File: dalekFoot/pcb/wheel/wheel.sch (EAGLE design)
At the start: 3 parts, among them IC1 LM1117MP-3.3

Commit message: add tb6612fng
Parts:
- added C3: 10uf, rcl:CPOL-US153CLV-0505
- added C4: 100uf, rcl:CPOL-US153CLV-0605
- added IC2: LM1117MP-3.3, lm1117:LM1117MP-3.3
- added U1: TB6612FNG(O,C,8,EL, TB6612FNG:TB6612FNG(O,C,8,EL
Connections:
- removed net VCC-3V3: C2.+, IC1.OUT
- new net VCC-ANALOG: C4.+, IC2.OUT
- new net VCC-DIGITAL: C2.+, IC1.OUT, U1.STBY, U1.VCC
- net BAT+: now also C3.+, IC2.IN
- net DGND: now also C3.-, C4.-, IC2.GND, U1.GND, U1.PGND1@1, U1.PGND1@2, U1.PGND2@1, U1.PGND2@2
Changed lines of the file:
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@@
 <setting verticaltext="up"/>
 </settings>
-<grid distance="0.1" unitdist="inch" unit="mil" style="dots" multiple="1" display="yes" altdistance="0.01" altunitdist="inch" altunit="mil"/>
+<grid distance="0.1" unitdist="inch" unit="inch" style="lines" multiple="1" display="yes" altdistance="0.01" altunitdist="inch" altunit="inch"/>
 <layers>
 <layer number="1" name="Top" color="4" fill="1" visible="no" active="no"/>
@@
 <part name="SUPPLY2" library="supply2" deviceset="DGND" device=""/>
 <part name="SUPPLY3" library="supply2" deviceset="DGND" device=""/>
+<part name="IC2" library="lm1117" deviceset="LM1117?-*" device="MP" technology="3.3"/>
+<part name="SUPPLY4" library="supply2" deviceset="DGND" device=""/>
+<part name="C3" library="rcl" deviceset="CPOL-US" device="153CLV-0505" value="10uf"/>
+<part name="C4" library="rcl" deviceset="CPOL-US" device="153CLV-0605" value="100uf"/>
+<part name="SUPPLY5" library="supply2" deviceset="DGND" device=""/>
+<part name="SUPPLY6" library="supply2" deviceset="DGND" device=""/>
+<part name="U1" library="TB6612FNG" deviceset="TB6612FNG(O,C,8,EL" device=""/>
+<part name="SUPPLY7" library="supply2" deviceset="DGND" device=""/>
 </parts>
 <sheets>
@@
 <instance part="SUPPLY2" gate="G$1" x="96.52" y="-63.5"/>
 <instance part="SUPPLY3" gate="G$1" x="63.5" y="-63.5"/>
+<instance part="IC2" gate="G$1" x="81.28" y="-81.28"/>
+<instance part="SUPPLY4" gate="G$1" x="81.28" y="-104.14"/>
+<instance part="C3" gate="G$1" x="63.5" y="-88.9"/>
+<instance part="C4" gate="G$1" x="96.52" y="-88.9"/>
+<instance part="SUPPLY5" gate="G$1" x="96.52" y="-104.14"/>
+<instance part="SUPPLY6" gate="G$1" x="63.5" y="-104.14"/>
+<instance part="U1" gate="G$1" x="426.72" y="-96.52"/>
+<instance part="SUPPLY7" gate="G$1" x="447.04" y="-134.62"/>
 </instances>
 <busses>
@@
 <pinref part="SUPPLY2" gate="G$1" pin="DGND"/>
 <wire x1="96.52" y1="-53.34" x2="96.52" y2="-60.96" width="0.1524" layer="91"/>
+</segment>
+<segment>
+<pinref part="IC2" gate="G$1" pin="GND"/>
+<pinref part="SUPPLY4" gate="G$1" pin="DGND"/>
+<wire x1="81.28" y1="-88.9" x2="81.28" y2="-101.6" width="0.1524" layer="91"/>
+</segment>
+<segment>
+<pinref part="SUPPLY6" gate="G$1" pin="DGND"/>
+<pinref part="C3" gate="G$1" pin="-"/>
+<wire x1="63.5" y1="-101.6" x2="63.5" y2="-93.98" width="0.1524" layer="91"/>
+</segment>
+<segment>
+<pinref part="C4" gate="G$1" pin="-"/>
+<pinref part="SUPPLY5" gate="G$1" pin="DGND"/>
+<wire x1="96.52" y1="-93.98" x2="96.52" y2="-101.6" width="0.1524" layer="91"/>
+</segment>
+<segment>
+<pinref part="U1" gate="G$1" pin="PGND2@2"/>
+<pinref part="SUPPLY7" gate="G$1" pin="DGND"/>
+<wire x1="441.96" y1="-114.3" x2="447.04" y2="-114.3" width="0.1524" layer="91"/>
+<wire x1="447.04" y1="-114.3" x2="447.04" y2="-116.84" width="0.1524" layer="91"/>
+<pinref part="U1" gate="G$1" pin="PGND2@1"/>
+<wire x1="447.04" y1="-116.84" x2="447.04" y2="-119.38" width="0.1524" layer="91"/>
+<wire x1="447.04" y1="-119.38" x2="447.04" y2="-121.92" width="0.1524" layer="91"/>
+<wire x1="447.04" y1="-121.92" x2="447.04" y2="-124.46" width="0.1524" layer="91"/>
+<wire x1="447.04" y1="-124.46" x2="447.04" y2="-132.08" width="0.1524" layer="91"/>
+<wire x1="441.96" y1="-116.84" x2="447.04" y2="-116.84" width="0.1524" layer="91"/>
+<junction x="447.04" y="-116.84"/>
+<pinref part="U1" gate="G$1" pin="PGND1@2"/>
+<wire x1="441.96" y1="-119.38" x2="447.04" y2="-119.38" width="0.1524" layer="91"/>
+<junction x="447.04" y="-119.38"/>
+<pinref part="U1" gate="G$1" pin="PGND1@1"/>
+<wire x1="441.96" y1="-121.92" x2="447.04" y2="-121.92" width="0.1524" layer="91"/>
+<junction x="447.04" y="-121.92"/>
+<pinref part="U1" gate="G$1" pin="GND"/>
+<wire x1="441.96" y1="-124.46" x2="447.04" y2="-124.46" width="0.1524" layer="91"/>
+<junction x="447.04" y="-124.46"/>
 </segment>
 </net>
@@
 <label x="53.34" y="-40.64" size="1.778" layer="95"/>
 </segment>
-</net>
-<net name="VCC-3V3" class="0">
+<segment>
+<pinref part="IC2" gate="G$1" pin="IN"/>
+<wire x1="53.34" y1="-81.28" x2="63.5" y2="-81.28" width="0.1524" layer="91"/>
+<pinref part="C3" gate="G$1" pin="+"/>
+<wire x1="63.5" y1="-81.28" x2="73.66" y2="-81.28" width="0.1524" layer="91"/>
+<wire x1="63.5" y1="-86.36" x2="63.5" y2="-81.28" width="0.1524" layer="91"/>
+<junction x="63.5" y="-81.28"/>
+<label x="53.34" y="-81.28" size="1.778" layer="95"/>
+</segment>
+</net>
+<net name="VCC-DIGITAL" class="0">
 <segment>
 <pinref part="IC1" gate="G$1" pin="OUT"/>
@@
 <label x="104.14" y="-40.64" size="1.778" layer="95"/>
 </segment>
-</net>
+<segment>
+<pinref part="U1" gate="G$1" pin="STBY"/>
+<wire x1="411.48" y1="-81.28" x2="398.78" y2="-81.28" width="0.1524" layer="91"/>
+<label x="396.24" y="-81.28" size="1.778" layer="95"/>
+</segment>
+<segment>
+<pinref part="U1" gate="G$1" pin="VCC"/>
+<wire x1="441.96" y1="-71.12" x2="452.12" y2="-71.12" width="0.1524" layer="91"/>
+<label x="449.58" y="-71.12" size="1.778" layer="95"/>
+</segment>
+</net>
+<net name="VCC-ANALOG" class="0">
+<segment>
+<pinref part="IC2" gate="G$1" pin="OUT"/>
+<wire x1="88.9" y1="-81.28" x2="96.52" y2="-81.28" width="0.1524" layer="91"/>
+<pinref part="C4" gate="G$1" pin="+"/>
+<wire x1="96.52" y1="-81.28" x2="109.22" y2="-81.28" width="0.1524" layer="91"/>
+<wire x1="96.52" y1="-86.36" x2="96.52" y2="-81.28" width="0.1524" layer="91"/>
+<junction x="96.52" y="-81.28"/>
+<label x="104.14" y="-81.28" size="1.778" layer="95"/>
+</segment>
+</net>

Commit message: add IR part
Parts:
- added C5: 10uf, rcl:CPOL-US153CLV-0505
- added C6: 100uf, rcl:CPOL-US153CLV-0605
- added D1, D2, D3: (no value), diode:DIODE-DO-214AC
- added IC3: LM1117MP-3.3, lm1117:LM1117MP-3.3
- added IC4, IC5: 4051D, 40xx:4051D
- added JP1: (no value), pinhead:PINHD-2X14
- added JP2: (no value), pinhead:PINHD-2X12
- added JP3: (no value), pinhead:PINHD-2X4
- added R1, R10, R11, R12, R13, R14, R15, R16, R17, R18, R19, R2, R20, R21, R22, R23, R24, R25, R26, R3, R4, R5, R6, R7, R8, R9: (no value), hqc:R-0603
- added U$1: STM32F4, stm32f4:STM32F4
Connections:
- new net N$1: D2.C, IC2.IN
- new net N$10: JP3.1
- new net N$11: JP1.6, R3.P$2
- new net N$12: JP1.8, R4.P$2
- new net N$13: JP1.10, R5.P$2
- new net N$14: JP1.12, R6.P$2
- new net N$15: JP1.14, R7.P$2
- new net N$16: JP1.16, R8.P$2
- new net N$17: JP1.18, R9.P$2
- new net N$18: JP1.20, R10.P$2
- new net N$19: JP1.22, R11.P$2
- new net N$2: U1.AO1@1, U1.AO1@2
- new net N$20: JP1.24, R12.P$2
- new net N$21: JP1.26, R13.P$2
- new net N$22: JP1.28, R14.P$2
- new net N$23: JP3.3
- new net N$24: JP2.2, R15.P$2
- new net N$25: JP2.4, R16.P$2
- new net N$26: JP2.6, R17.P$2
- new net N$27: JP2.8, R18.P$2
- new net N$28: JP2.10, R19.P$2
- new net N$29: JP2.12, R20.P$2
- new net N$3: U1.AO2@1, U1.AO2@2
- new net N$30: JP2.14, R21.P$2
- new net N$31: JP2.16, R22.P$2
- new net N$32: JP2.18, R23.P$2
- new net N$33: JP2.20, R24.P$2
- new net N$34: JP2.22, R25.P$2
- new net N$35: JP2.24, R26.P$2
- new net N$36: JP3.5
- new net N$37: JP3.7
- new net N$38: D3.C, IC3.IN
- new net N$39: IC4A.X0
- new net N$4: IC4A.X3
- new net N$40: IC4A.X1
- new net N$41: IC4A.X2
- new net N$42: IC4A.X4
- new net N$43: IC4A.X5
- new net N$44: IC4A.X6
- new net N$45: IC4A.X7
- new net N$46: IC4A.X
- new net N$47: IC5A.X0
- new net N$48: IC5A.X1
- new net N$49: IC5A.X2
- new net N$5: D1.C, IC1.IN
- new net N$50: IC5A.X3
- new net N$51: IC5A.X4
- new net N$52: IC5A.X5
- new net N$53: IC5A.X6
- new net N$54: IC5A.X7
- new net N$55: IC5A.X
- new net N$6: U1.BO1@1, U1.BO1@2
- new net N$7: JP1.2, R1.P$2
- new net N$8: U1.BO2@1, U1.BO2@2
- new net N$9: JP1.4, R2.P$2
- new net SWCLK: U$1.P$A14
- new net SWDIO: U$1.P$A13
- new net VCC-IR: C6.+, IC3.OUT, IC4P.VCC, IC5P.VCC, JP1.1, JP1.11, JP1.13, JP1.15, JP1.17, JP1.19, JP1.21, JP1.23, JP1.25, JP1.27, JP1.3, JP1.5, JP1.7, JP1.9, JP2.1, JP2.11, JP2.13, JP2.15, JP2.17, JP2.19, JP2.21, JP2.23, JP2.3, JP2.5, JP2.7, JP2.9
- net BAT+: now also C5.+, D1.A, D2.A, D3.A, U1.VM1, U1.VM2, U1.VM3; no longer IC1.IN, IC2.IN
- net DGND: now also C5.-, C6.-, IC3.GND, IC4A.INH, IC4P.GND, IC4P.VEE, IC5A.INH, IC5P.GND, IC5P.VEE, JP3.2, JP3.4, JP3.6, JP3.8, R1.P$1, R10.P$1, R11.P$1, R12.P$1, R13.P$1, R14.P$1, R15.P$1, R16.P$1, R17.P$1, R18.P$1, R19.P$1, R2.P$1, R20.P$1, R21.P$1, R22.P$1, R23.P$1, R24.P$1, R25.P$1, R26.P$1, R3.P$1, R4.P$1, R5.P$1, R6.P$1, R7.P$1, R8.P$1, R9.P$1, U$1.P$GND
- net VCC-DIGITAL: now also U$1.P$3V3
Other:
- moved on the sheet: C1, C3, U1

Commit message: IR and SPI finsihed
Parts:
- added JP4: (no value), pinhead:PINHD-2X3
- added R27: (no value), rcl:R-EU_R0402
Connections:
- net N$34 renamed IR24
- net N$49 renamed IR24\
- removed net N$10: JP3.1
- removed net N$11: JP1.6, R3.P$2
- removed net N$12: JP1.8, R4.P$2
- removed net N$13: JP1.10, R5.P$2
- removed net N$14: JP1.12, R6.P$2
- removed net N$15: JP1.14, R7.P$2
- removed net N$16: JP1.16, R8.P$2
- removed net N$17: JP1.18, R9.P$2
- removed net N$18: JP1.20, R10.P$2
- removed net N$19: JP1.22, R11.P$2
- removed net N$20: JP1.24, R12.P$2
- removed net N$21: JP1.26, R13.P$2
- removed net N$22: JP1.28, R14.P$2
- removed net N$23: JP3.3
- removed net N$24: JP2.2, R15.P$2
- removed net N$25: JP2.4, R16.P$2
- removed net N$26: JP2.6, R17.P$2
- removed net N$27: JP2.8, R18.P$2
- removed net N$28: JP2.10, R19.P$2
- removed net N$29: JP2.12, R20.P$2
- removed net N$30: JP2.14, R21.P$2
- removed net N$31: JP2.16, R22.P$2
- removed net N$32: JP2.18, R23.P$2
- removed net N$33: JP2.20, R24.P$2
- removed net N$35: JP2.24, R26.P$2
- removed net N$36: JP3.5
- removed net N$37: JP3.7
- removed net N$39: IC4A.X0
- removed net N$40: IC4A.X1
- removed net N$41: IC4A.X2
- removed net N$42: IC4A.X4
- removed net N$43: IC4A.X5
- removed net N$44: IC4A.X6
- removed net N$45: IC4A.X7
- removed net N$46: IC4A.X
- removed net N$47: IC5A.X0
- removed net N$48: IC5A.X1
- removed net N$50: IC5A.X3
- removed net N$51: IC5A.X4
- removed net N$52: IC5A.X5
- removed net N$53: IC5A.X6
- removed net N$54: IC5A.X7
- removed net N$55: IC5A.X
- removed net N$7: JP1.2, R1.P$2
- removed net N$9: JP1.4, R2.P$2
- new net AIN0: IC5A.X4, JP3.1
- new net AIN1: IC5A.X5, JP3.3
- new net AIN2: IC5A.X6, JP3.5
- new net AIN3: IC5A.X7, JP3.7
- new net IR0: JP1.2, R1.P$2, U$1.P$A0
- new net IR1: JP1.4, R2.P$2, U$1.P$A1
- new net IR10: JP1.22, R11.P$2, U$1.P$C0
- new net IR11: JP1.24, R12.P$2, U$1.P$C1
- new net IR12: JP1.26, R13.P$2, U$1.P$C2
- new net IR13: JP1.28, R14.P$2, U$1.P$C3
- new net IR14: IC4A.X0, JP2.2, R15.P$2
- new net IR15: IC4A.X1, JP2.4, R16.P$2
- new net IR16: IC4A.X2, JP2.6, R17.P$2
- new net IR17: IC4A.X3, JP2.8, R18.P$2
- new net IR18: IC4A.X4, JP2.10, R19.P$2
- new net IR19: IC4A.X5, JP2.12, R20.P$2
- new net IR2: JP1.6, R3.P$2, U$1.P$A2
- new net IR20: IC4A.X6, JP2.14, R21.P$2
- new net IR21: IC4A.X7, JP2.16, R22.P$2
- new net IR22: IC5A.X0, JP2.18, R23.P$2
- new net IR23: IC5A.X1, JP2.20, R24.P$2
- new net IR25: IC5A.X3, JP2.24, R26.P$2
- new net IR3: JP1.8, R4.P$2, U$1.P$A3
- new net IR4: JP1.10, R5.P$2, U$1.P$A4
- new net IR5: JP1.12, R6.P$2, U$1.P$A5
- new net IR6: JP1.14, R7.P$2, U$1.P$A6
- new net IR7: JP1.16, R8.P$2, U$1.P$A7
- new net IR8: JP1.18, R9.P$2, U$1.P$B0
- new net IR9: JP1.20, R10.P$2, U$1.P$B1
- new net N$56: IC4A.A
- new net N$57: IC4A.B
- new net N$59: IC5A.A
- new net N$60: IC5A.B
- new net N$61: IC5A.C
- new net PC4_AIN: IC4A.X, U$1.P$C4
- new net PC5_AIN: IC5A.X, U$1.P$C5
- new net SPI_MISO: JP4.2, U$1.P$B14
- new net SPI_MOSI: JP4.4, U$1.P$B15
- new net SPI_NSS: JP4.5, U$1.P$B12
- new net SPI_SCK: JP4.3, U$1.P$B13
- net DGND: now also JP4.6
- net N$4: now also JP4.1, R27.2; no longer IC4A.X3
- net VCC-DIGITAL: now also R27.1

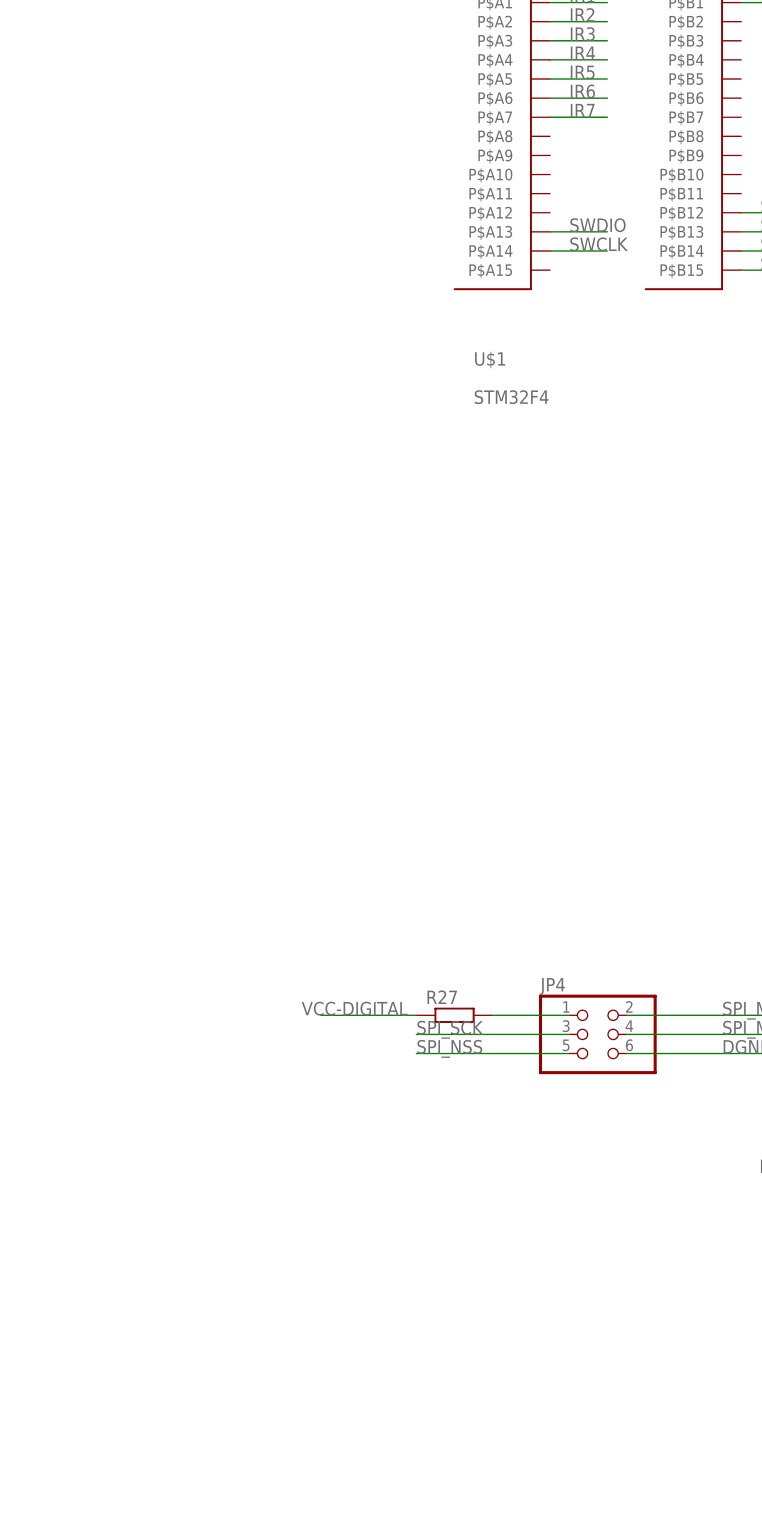
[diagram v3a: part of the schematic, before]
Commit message: add usart and swd port on schematic
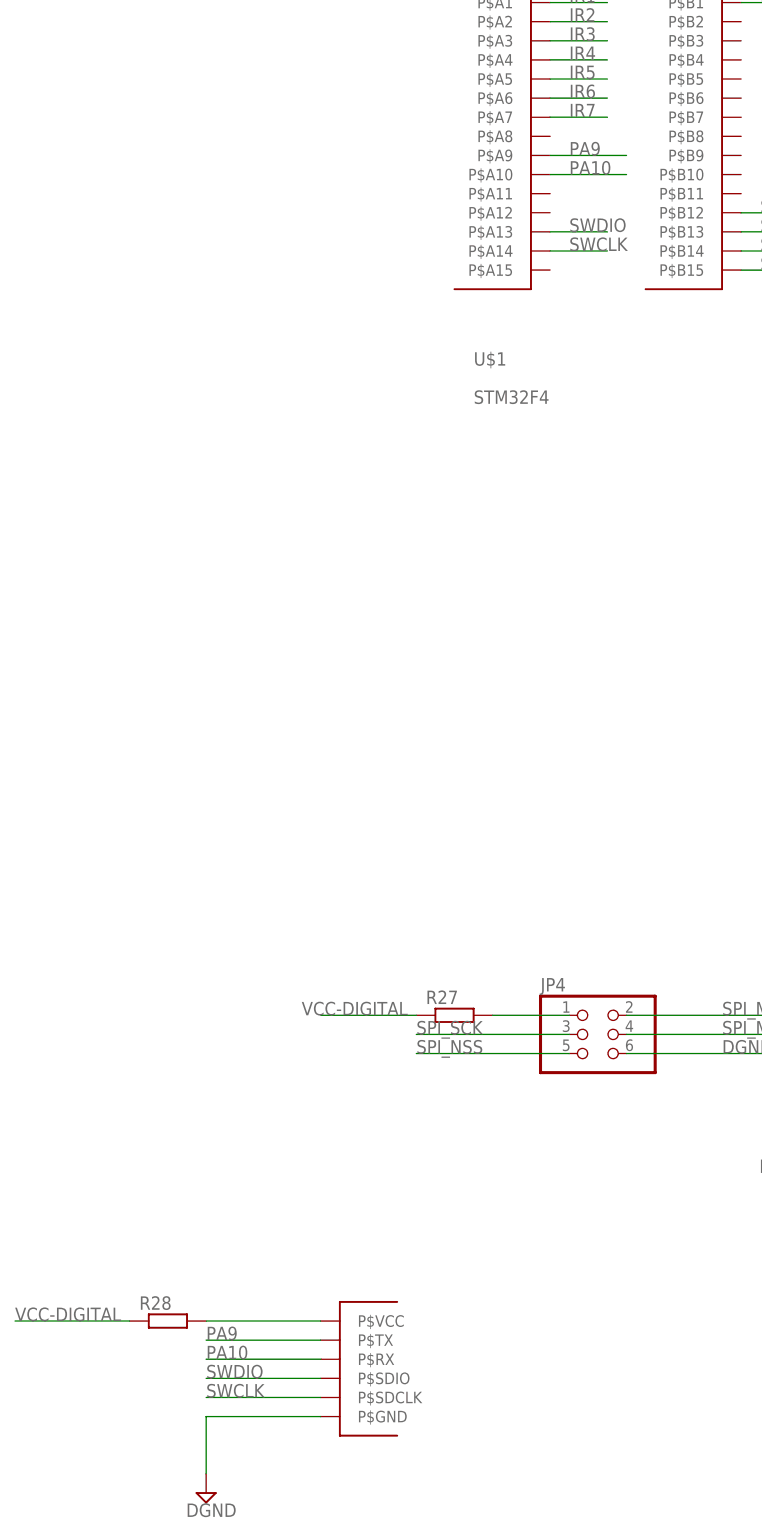
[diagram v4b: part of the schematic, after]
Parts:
- added J1: (no value), hqc:DEBUG-PORT
- added R28: (no value), rcl:R-EU_R0402
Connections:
- new net N$7: J1.P$VCC, R28.2
- new net PA10: J1.P$RX, U$1.P$A10
- new net PA9: J1.P$TX, U$1.P$A9
- net DGND: now also J1.P$GND
- net SWCLK: now also J1.P$SDCLK
- net SWDIO: now also J1.P$SDIO
- net VCC-DIGITAL: now also R28.1
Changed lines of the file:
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@@
 <part name="R27" library="rcl" deviceset="R-EU_" device="R0402"/>
 <part name="SUPPLY19" library="supply2" deviceset="DGND" device=""/>
+<part name="J1" library="hqc" deviceset="DEBUG-PORT" device=""/>
+<part name="R28" library="rcl" deviceset="R-EU_" device="R0402"/>
+<part name="SUPPLY20" library="supply2" deviceset="DGND" device=""/>
 </parts>
 <sheets>
@@
 <instance part="R27" gate="G$1" x="50.8" y="-391.16"/>
 <instance part="SUPPLY19" gate="G$1" x="93.98" y="-408.94"/>
+<instance part="J1" gate="G$1" x="40.64" y="-439.42"/>
+<instance part="R28" gate="G$1" x="12.7" y="-431.8"/>
+<instance part="SUPPLY20" gate="G$1" x="17.78" y="-454.66"/>
 </instances>
 <busses>
@@
 <wire x1="93.98" y1="-396.24" x2="93.98" y2="-406.4" width="0.1524" layer="91"/>
 </segment>
+<segment>
+<pinref part="J1" gate="G$1" pin="P$GND"/>
+<wire x1="17.78" y1="-444.5" x2="33.02" y2="-444.5" width="0.1524" layer="91"/>
+<wire x1="17.78" y1="-444.5" x2="17.78" y2="-452.12" width="0.1524" layer="91"/>
+<pinref part="SUPPLY20" gate="G$1" pin="DGND"/>
+</segment>
 </net>
 <net name="BAT+" class="0">
@@
 <label x="30.48" y="-391.16" size="1.778" layer="95"/>
 </segment>
+<segment>
+<pinref part="R28" gate="G$1" pin="1"/>
+<wire x1="7.62" y1="-431.8" x2="-7.62" y2="-431.8" width="0.1524" layer="91"/>
+<label x="-7.62" y="-431.8" size="1.778" layer="95"/>
+</segment>
 </net>
 <net name="VCC-ANALOG" class="0">
@@
 <label x="66.04" y="-287.02" size="1.778" layer="95"/>
 </segment>
+<segment>
+<pinref part="J1" gate="G$1" pin="P$SDIO"/>
+<wire x1="17.78" y1="-439.42" x2="33.02" y2="-439.42" width="0.1524" layer="91"/>
+<label x="17.78" y="-439.42" size="1.778" layer="95"/>
+</segment>
 </net>
 <net name="SWCLK" class="0">
@@
 <wire x1="63.5" y1="-289.56" x2="71.12" y2="-289.56" width="0.1524" layer="91"/>
 <label x="66.04" y="-289.56" size="1.778" layer="95"/>
+</segment>
+<segment>
+<pinref part="J1" gate="G$1" pin="P$SDCLK"/>
+<wire x1="33.02" y1="-441.96" x2="17.78" y2="-441.96" width="0.1524" layer="91"/>
+<label x="17.78" y="-441.96" size="1.778" layer="95"/>
 </segment>
 </net>
@@
 </segment>
 </net>
+<net name="N$7" class="0">
+<segment>
+<pinref part="J1" gate="G$1" pin="P$VCC"/>
+<wire x1="33.02" y1="-431.8" x2="17.78" y2="-431.8" width="0.1524" layer="91"/>
+<pinref part="R28" gate="G$1" pin="2"/>
+</segment>
+</net>
+<net name="PA9" class="0">
+<segment>
+<pinref part="J1" gate="G$1" pin="P$TX"/>
+<wire x1="17.78" y1="-434.34" x2="33.02" y2="-434.34" width="0.1524" layer="91"/>
+<label x="17.78" y="-434.34" size="1.778" layer="95"/>
+</segment>
+<segment>
+<pinref part="U$1" gate="G$1" pin="P$A9"/>
+<wire x1="63.5" y1="-276.86" x2="73.66" y2="-276.86" width="0.1524" layer="91"/>
+<label x="66.04" y="-276.86" size="1.778" layer="95"/>
+</segment>
+</net>
+<net name="PA10" class="0">
+<segment>
+<pinref part="J1" gate="G$1" pin="P$RX"/>
+<wire x1="33.02" y1="-436.88" x2="17.78" y2="-436.88" width="0.1524" layer="91"/>
+<label x="17.78" y="-436.88" size="1.778" layer="95"/>
+</segment>
+<segment>
+<pinref part="U$1" gate="G$1" pin="P$A10"/>
+<wire x1="63.5" y1="-279.4" x2="73.66" y2="-279.4" width="0.1524" layer="91"/>
+<label x="66.04" y="-279.4" size="1.778" layer="95"/>
+</segment>
+</net>
